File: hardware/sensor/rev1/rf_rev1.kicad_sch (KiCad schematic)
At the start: 27 parts

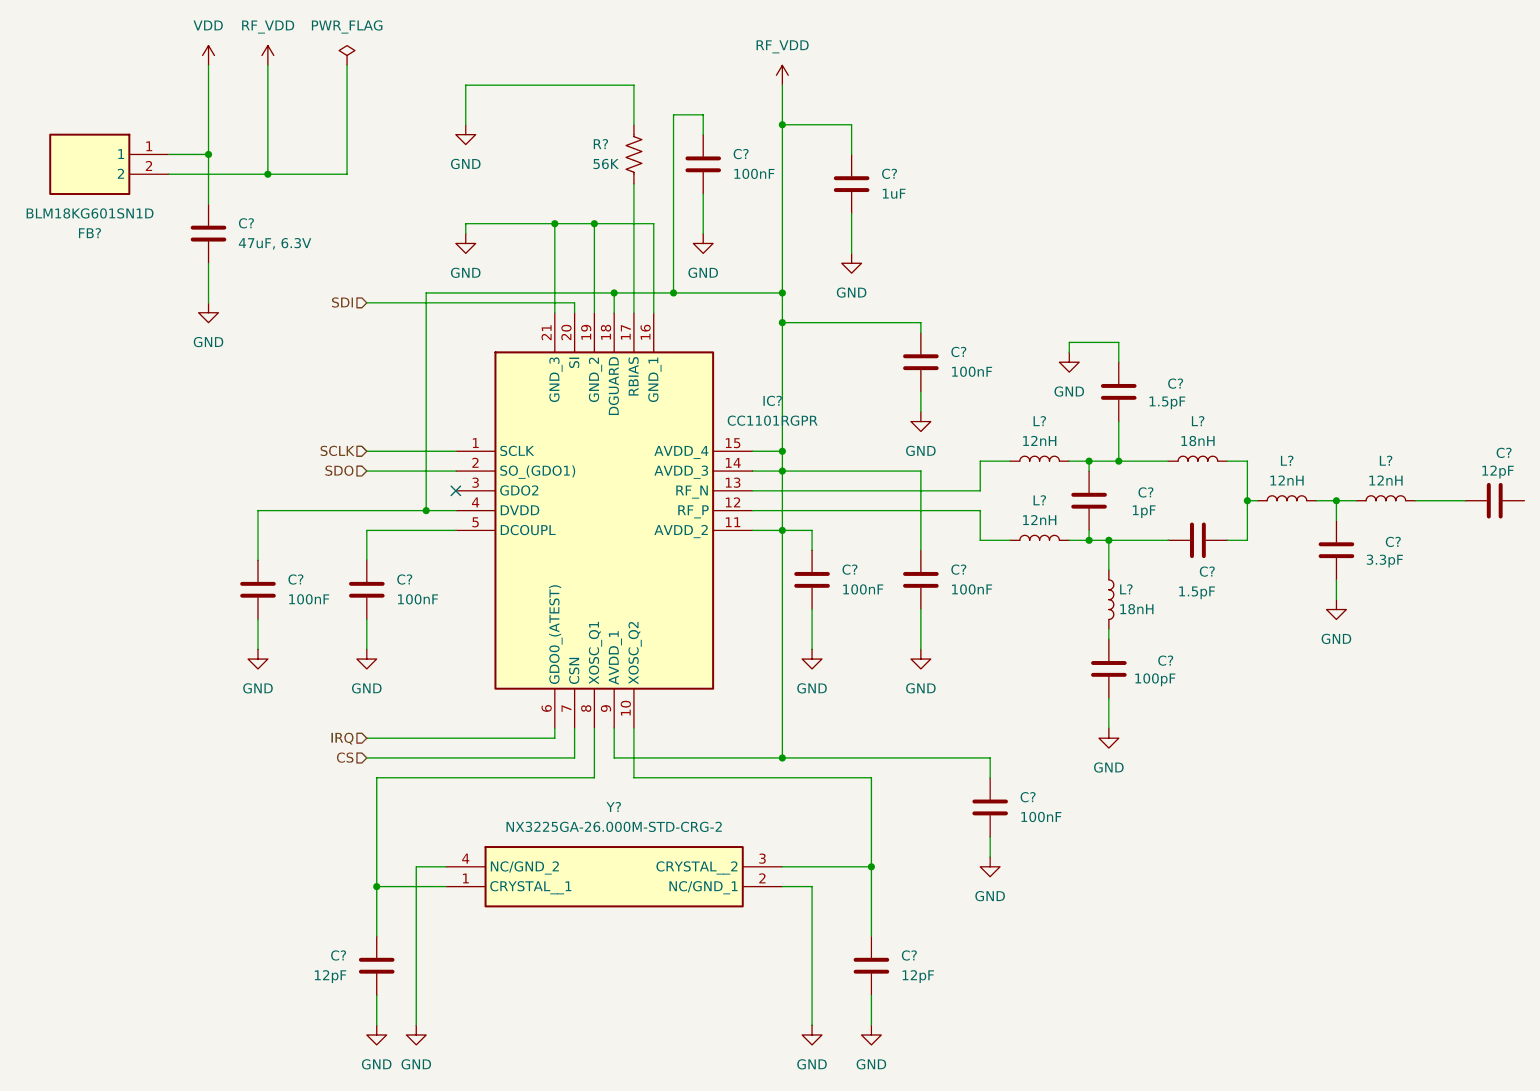
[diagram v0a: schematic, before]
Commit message: EG-49 Several components addes, such as bulk capacitors, battery holder, MCU and reed switches.
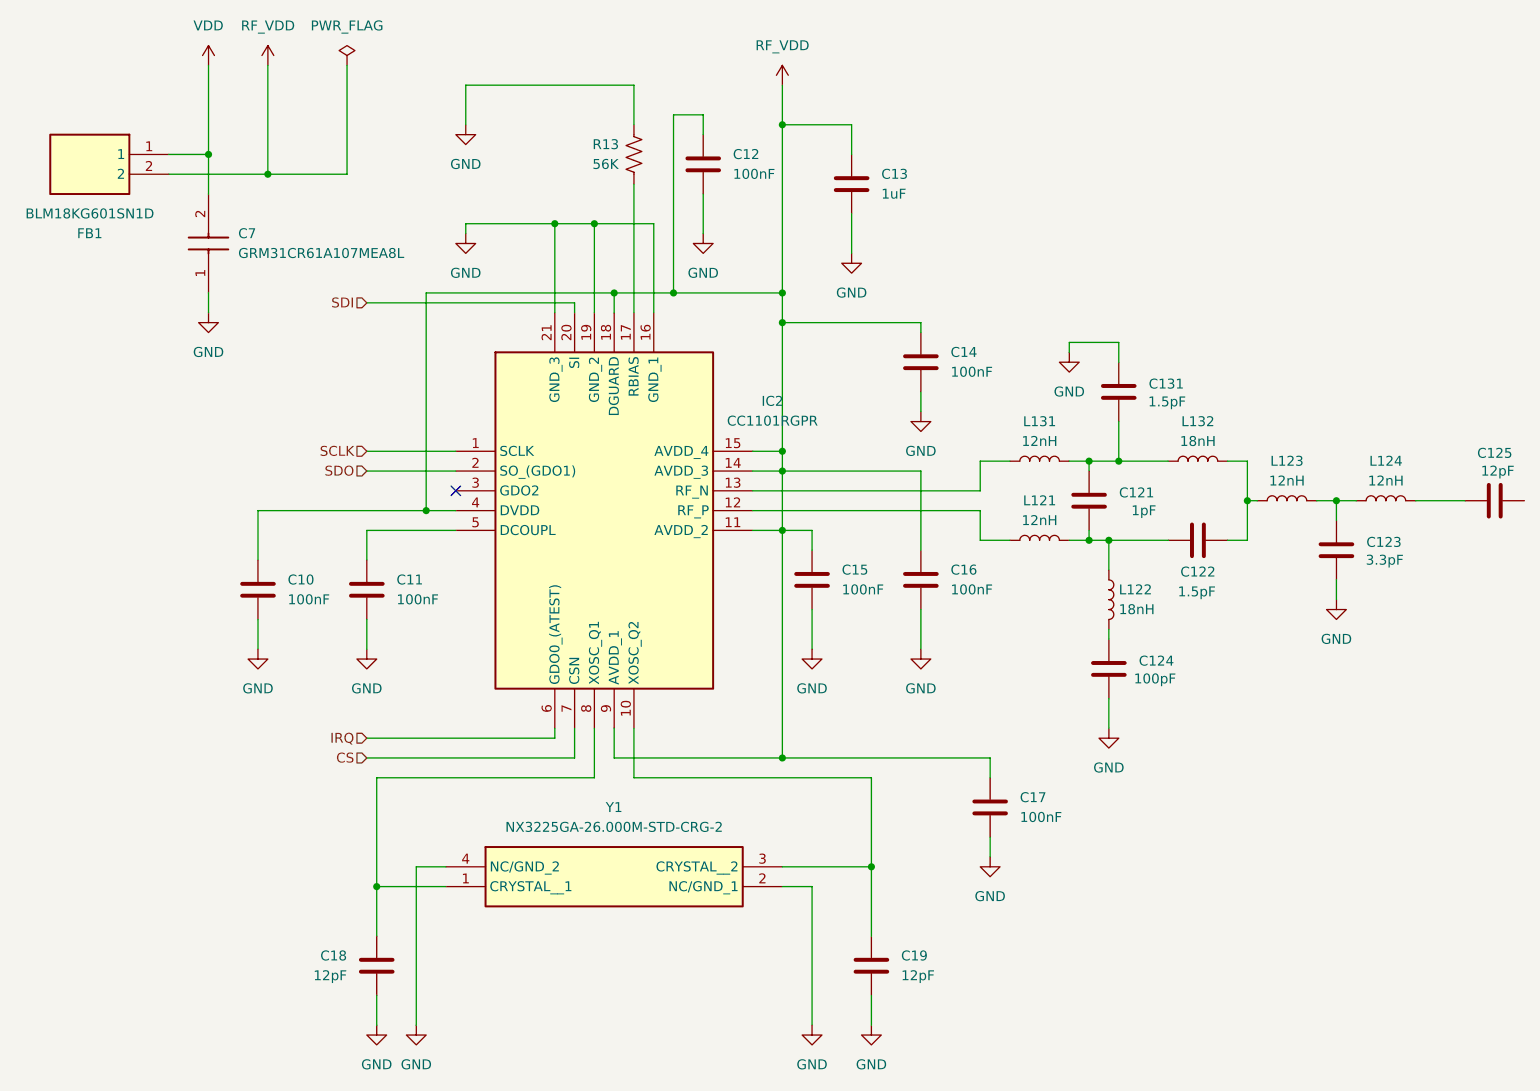
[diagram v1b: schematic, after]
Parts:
- removed C?: 47uF, 6.3V, Capacitor_SMD:C_1206_3216Metric, symbol Device:C
- added C7: GRM31CR61A107MEA8L, GRM31x, symbol GRM31CR61A107MEA8L:GRM31CR61A107MEA8L
- gave numbers to parts that had none: 26
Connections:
- net GND: now also C7.1
- net VDD: now also C7.2
